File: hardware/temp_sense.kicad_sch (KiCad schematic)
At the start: 42 parts, among them U2 CD4052B, U3 MCP6004, U4 CD4052B, U5 MCP6004

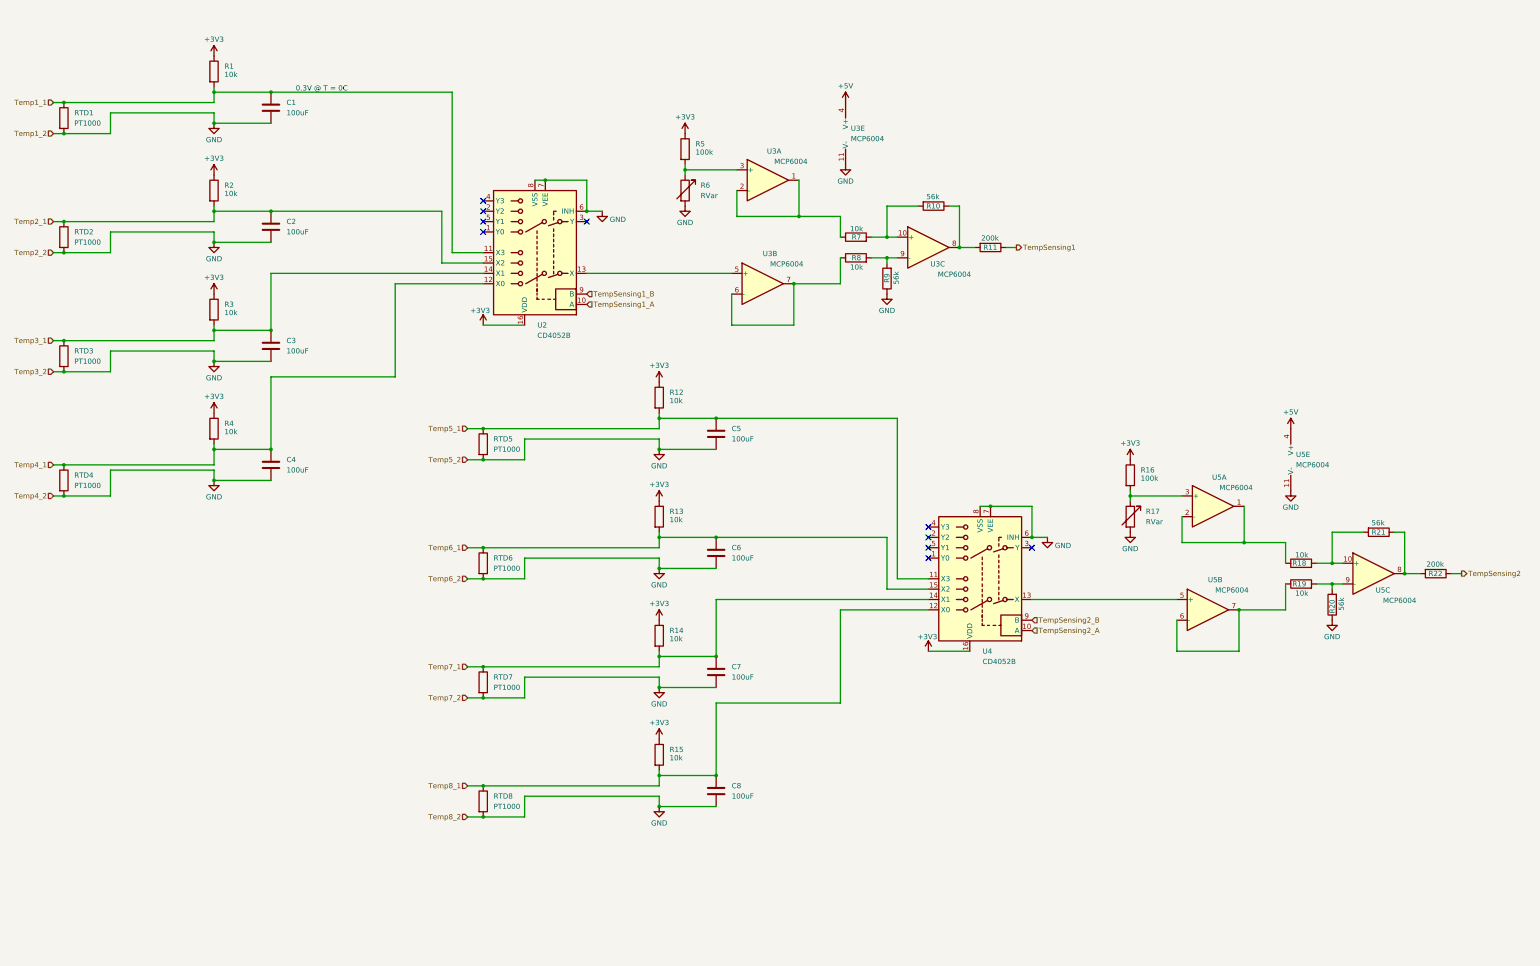
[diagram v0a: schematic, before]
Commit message: completed main board schematic
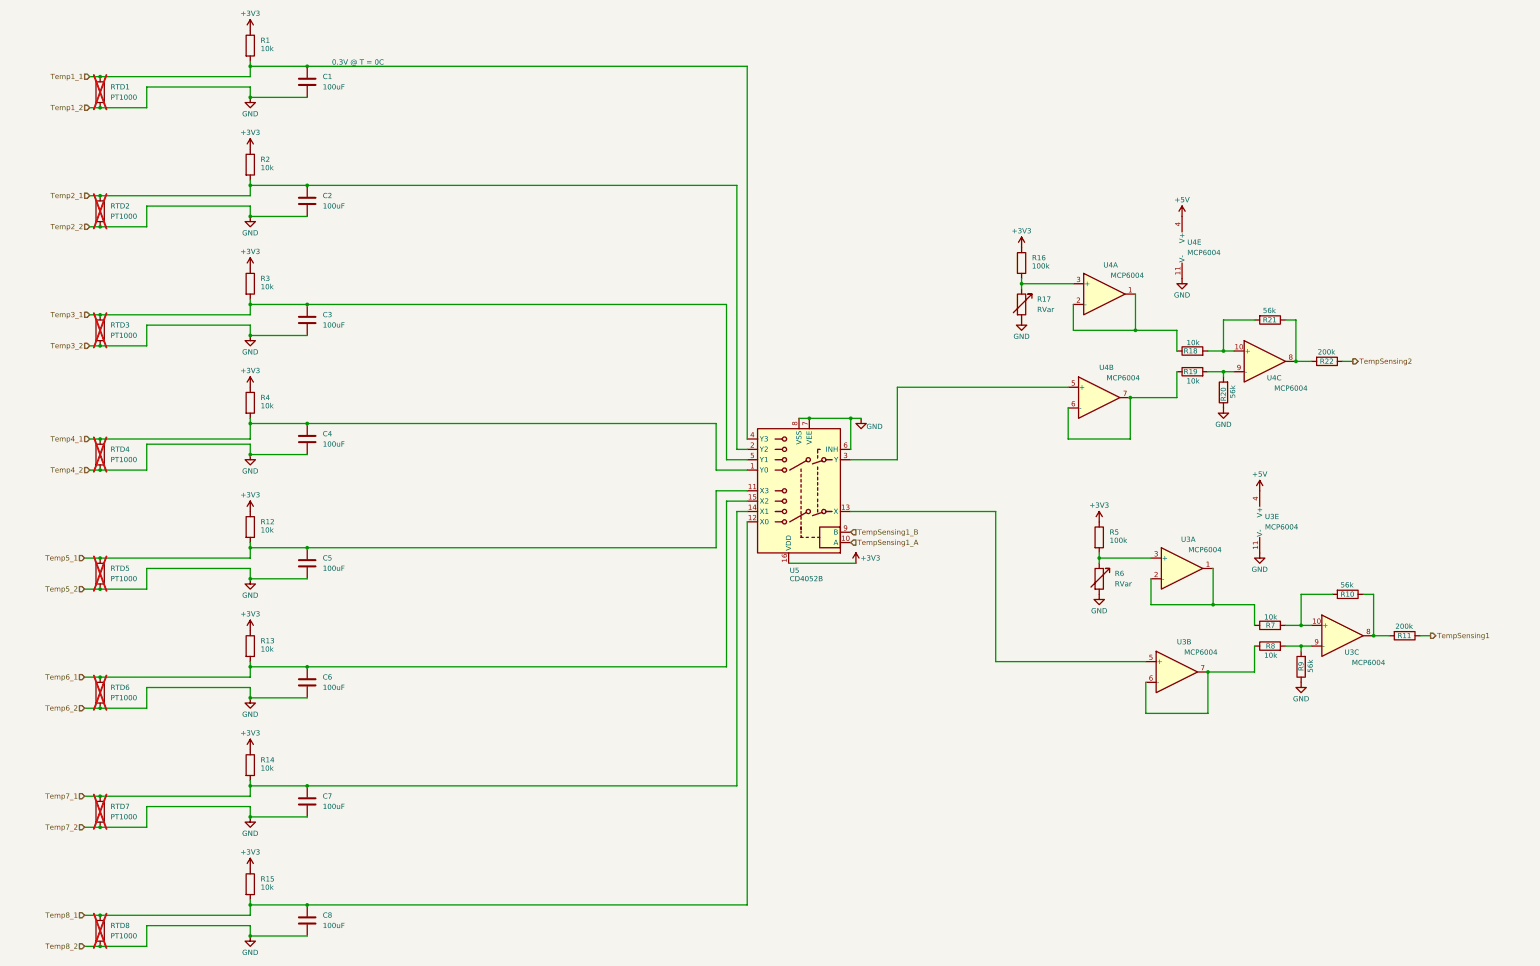
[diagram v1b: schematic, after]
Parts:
- removed U2, U4: CD4052B, symbol Analog_Switch:CD4052B
- removed U5: MCP6004, symbol Amplifier_Operational:MCP6004
- added U4: MCP6004, symbol Amplifier_Operational:MCP6004
- added U5: CD4052B, symbol Analog_Switch:CD4052B
- RTD1, RTD2, RTD3, RTD4, RTD5, RTD6, RTD7, RTD8: now not fitted
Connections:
- net +3V3: now also U5.16 (VDD)
- net +5V: now also U4.4 (V+)
- net GND: now also U4.11 (V-), U5.6 (INH), U5.7 (VEE), U5.8 (VSS)
- net Temp1_1: now also U5.4 (Y3)
- net Temp2_1: now also U5.2 (Y2)
- net Temp3_1: now also U5.5 (Y1)
- net Temp4_1: now also U5.1 (Y0)
- net Temp5_1: now also U5.11 (X3)
- net Temp6_1: now also U5.15 (X2)
- net Temp7_1: now also U5.14 (X1)
- net Temp8_1: now also U5.12 (X0)
- net TempSensing1_A: now also U5.10 (A)
- net TempSensing1_B: now also U5.9 (B)
- net at R16.2, R17.1: now also U4.3 (+)
- net at R18.1: now also U4.1, U4.2 (-)
- net at R18.2, R21.2: now also U4.10 (+)
- net at R19.1: now also U4.6 (-), U4.7
- net at R19.2, R20.2: now also U4.9 (-)
- net at U3.5 (+): now also U5.13 (X)
- net at R21.1, R22.2: now also U4.8
- new net: U4.5 (+), U5.3 (Y)
- no-connect marks 10 -> 0
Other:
- moved on the sheet: C1, C2, C3, C4, C5, C6, C7, C8, R1, R10, R11, R12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

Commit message: initial layout, power traces remain
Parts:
- C1, C2, C3, C4, C5, C6, C7, C8: footprint (none) -> Capacitor_SMD:C_0805_2012Metric_Pad1.18x1.45mm_HandSolder
- R1, R10, R11, R12, R13, R14, R15, R16, R18, R19, R2, R20, R21, R22, R3, R4, R5, R7, R8, R9: footprint (none) -> Resistor_SMD:R_0805_2012Metric_Pad1.20x1.40mm_HandSolder
- R17, R6: footprint (none) -> Potentiometer_THT:Potentiometer_Bourns_3296W_Vertical
- U3, U4: footprint (none) -> Package_SO:SOIC-14_3.9x8.7mm_P1.27mm
- U5: footprint (none) -> Package_SO:TSSOP-16_4.4x5mm_P0.65mm

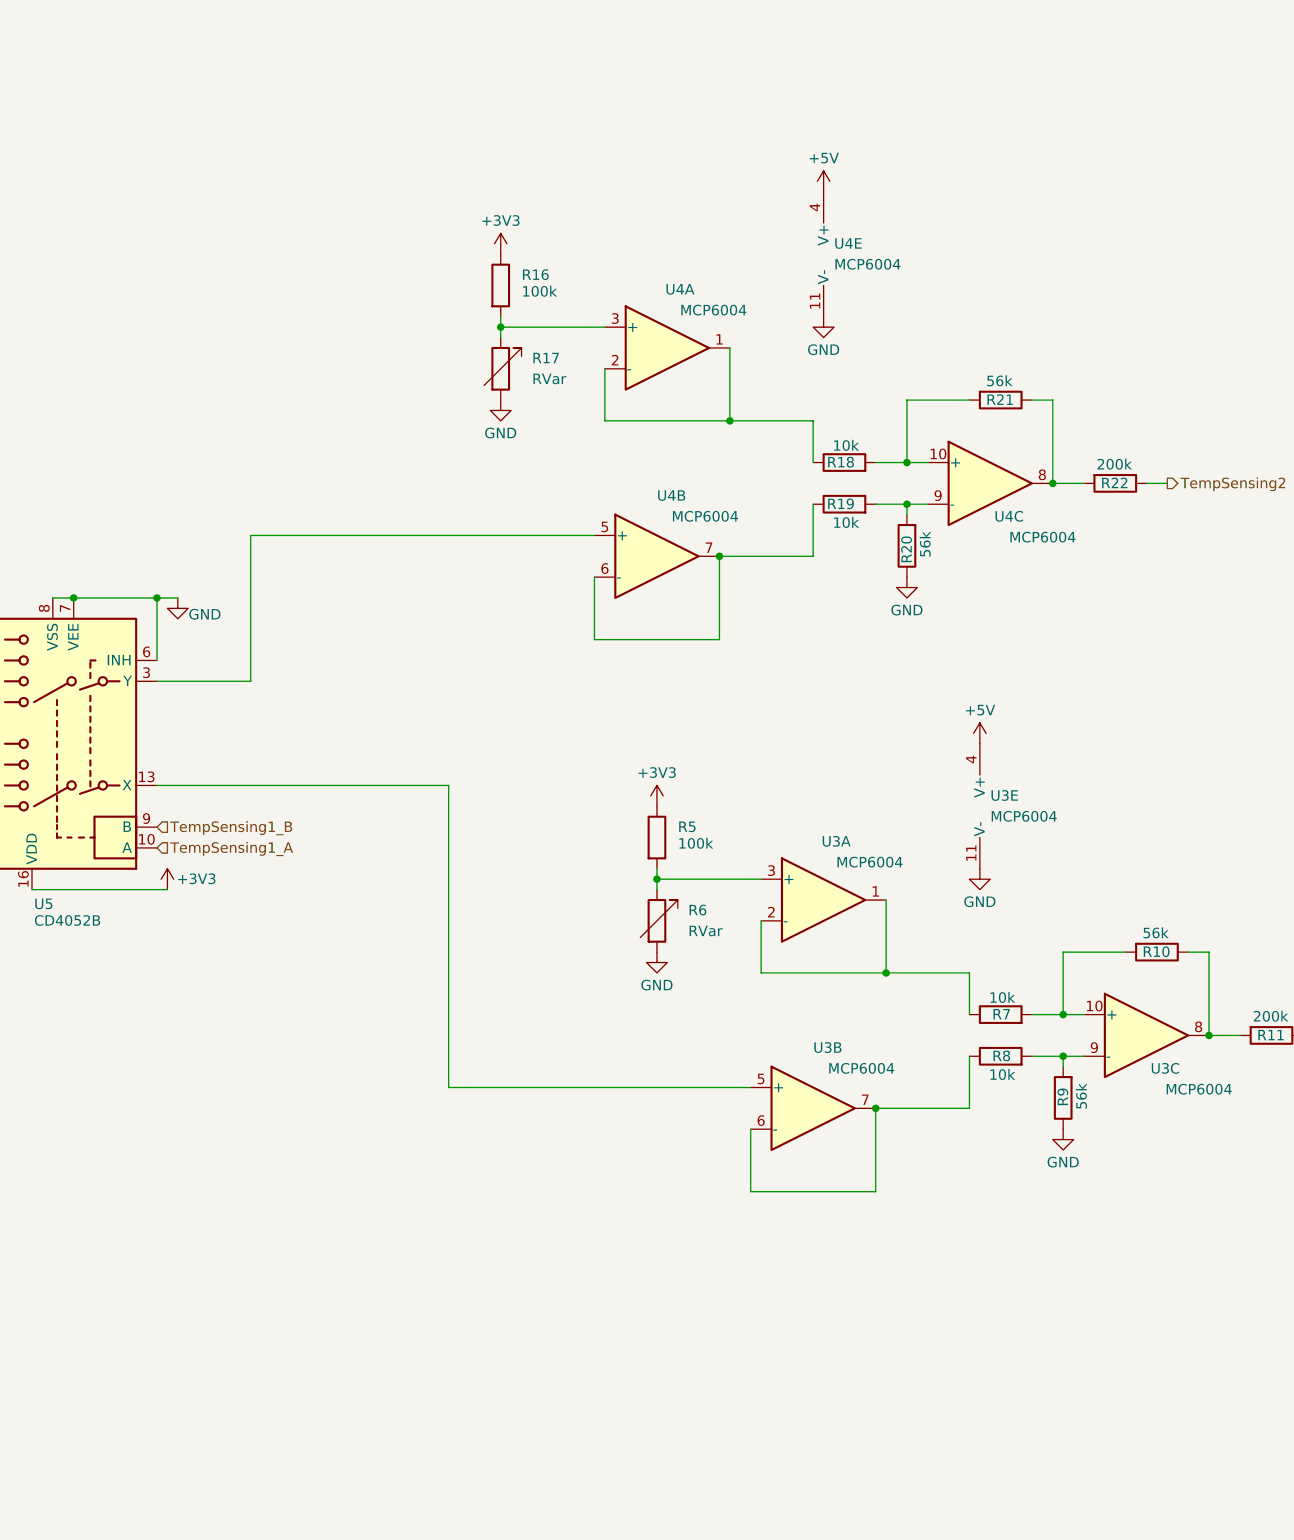
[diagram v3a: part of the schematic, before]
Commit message: Finished Layout and routing
* Flipped CAN transceiver upside down on schematic
* Moved CAN transceiver nearer to J13 and MCU CAN pins
* Moved 5V DCDC caps nearer to 5V DCDC
* Moved Silkscreen out from under U9
* Moved J2 and J1 to prevent plugging 12V into a temp sensor connector
* Change +3.3V to +3V3 to match MCU page
* Changed Current Sense circuit to use U4D, sharing with Temp Sense (for easier assembly)
* Placed Unused MCP6004s on schematic and connected them per datasheet fig 4-5
* Remove connections to HV- in Current Sensing (Replaced with GND)
* Tightened up Temp and Current Sense amplifier layouts
* Swap U15A with U15D for easier routing
* Added buffer to voltage sense circuit because filter stage could significantly load the voltage divider
* Added a smattering of decoupling caps
* Finished Layout and routing
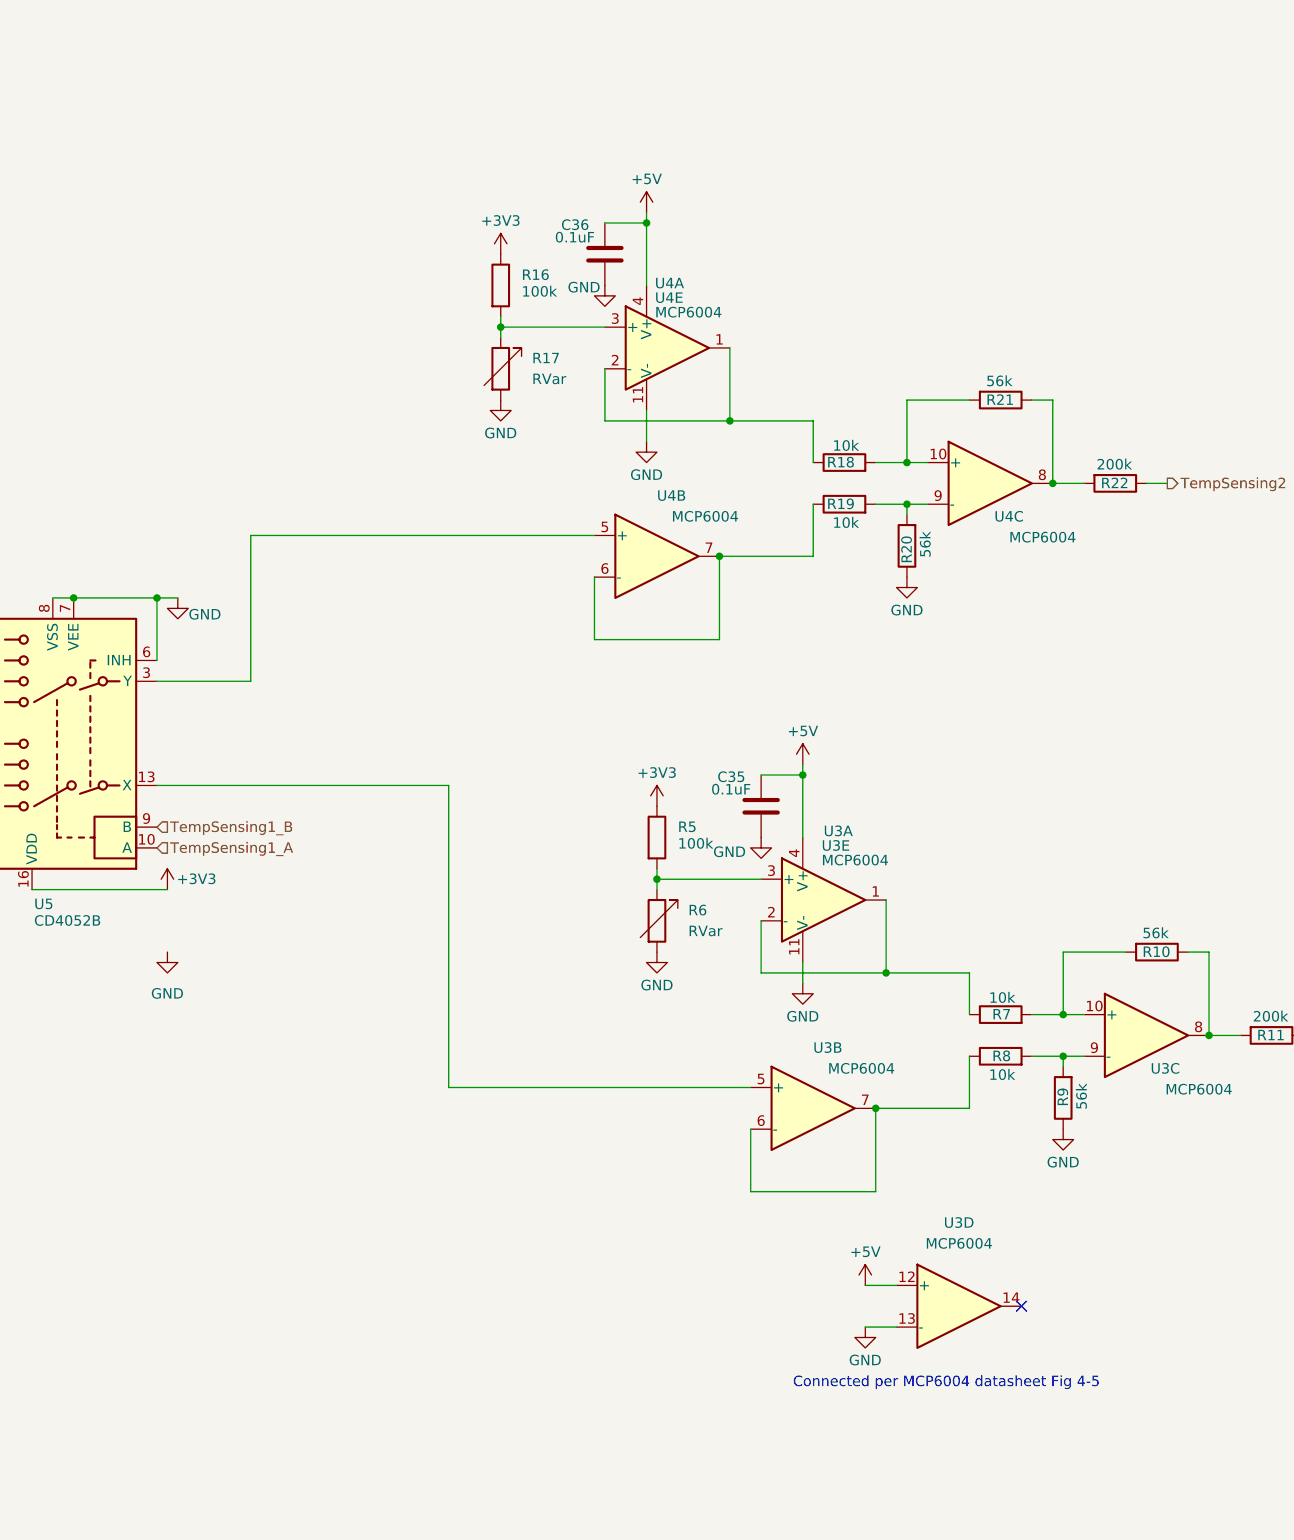
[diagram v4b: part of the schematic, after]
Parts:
- added C35, C36: 0.1uF, Capacitor_SMD:C_0805_2012Metric_Pad1.18x1.45mm_HandSolder, symbol Device:C
- C1, C2, C3, C4, C5, C6, C7, C8, R1, R10, R11, R12, R13, R14, R15, R16, R18, R19, R2, R20, R21, R22, R3, R4, R5, R7, R8, R9: KiLib_Generator (none) -> SMD_2terminal_chip_molded
- R17, R6: KiLib_Generator (none) -> potentiometer/THT
- U3, U4, U5: KiLib_Generator (none) -> package/gullwing
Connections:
- net +5V: now also U3.12 (+), C35.1, C36.1
- net GND: now also U3.13 (-), C35.2, C36.2
- no-connect marks 0 -> 1
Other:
- note added: "Connected per MCP6004 datasheet Fig 4-5"
- moved on the sheet: U3E, U4E

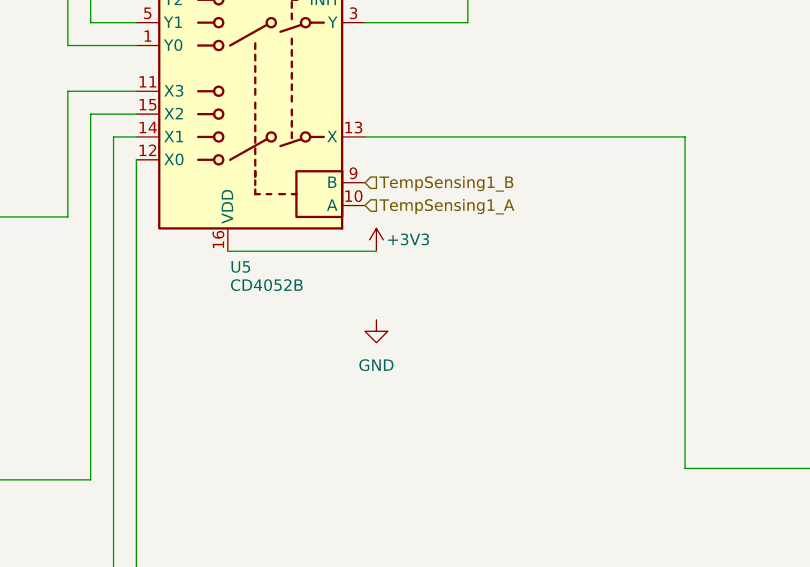
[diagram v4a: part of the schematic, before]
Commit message: Fix up silkscreen, testpoints, and one more decoupler
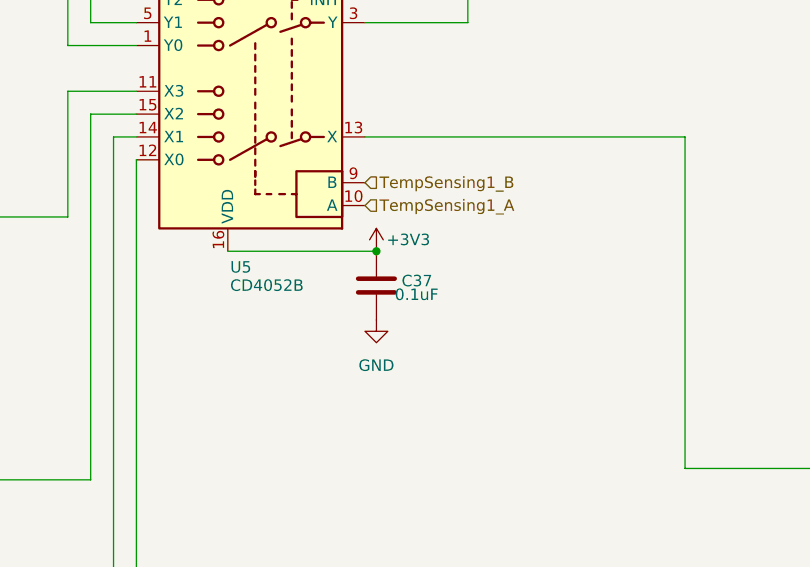
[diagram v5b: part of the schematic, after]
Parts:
- added C37: 0.1uF, Capacitor_SMD:C_0805_2012Metric_Pad1.18x1.45mm_HandSolder, symbol Device:C
- added unit 4 of U3
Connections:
- net +3V3: now also C37.1
- net +5V: now also U3.12 (+); no longer U3.12 (+)
- net GND: now also C37.2, U3.13 (-); no longer U3.13 (-)
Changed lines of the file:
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@@
 	)
 	(junction
+		(at 229.87 161.29)
+		(diameter 0)
+		(color 0 0 0 0)
+	)
+	(junction
 		(at 307.34 147.32)
 		(diameter 0)
@@
 					(unit 1)
 				)
+			)
+		)
+	)
+	(symbol
+		(lib_id "Device:C")
+		(at 229.87 165.1 0)
+		(mirror y)
+		(unit 1)
+		(body_style 1)
+		(exclude_from_sim no)
+		(in_bom yes)
+		(on_board yes)
+		(in_pos_files yes)
+		(dnp no)
+		(property "Reference" "C37"
+			(at 232.664 164.592 0)
+			(show_name no)
+			(do_not_autoplace no)
+			(effects
+				(font
+					(size 1.27 1.27)
+				)
+				(justify right)
+			)
+		)
+		(property "Value" "0.1uF"
+			(at 231.902 166.116 0)
+			(show_name no)
+			(do_not_autoplace no)
+			(effects
+				(font
+					(size 1.27 1.27)
+				)
+				(justify right)
+			)
+		)
+		(property "Footprint" "Capacitor_SMD:C_0805_2012Metric_Pad1.18x1.45mm_HandSolder"
+			(at 228.9048 168.91 0)
+			(hide yes)
+			(show_name no)
+			(do_not_autoplace no)
+			(effects
+				(font
+					(size 1.27 1.27)
+				)
+			)
+		)
+		(property "Datasheet" ""
+			(at 229.87 165.1 0)
+			(hide yes)
+			(show_name no)
+			(do_not_autoplace no)
+			(effects
+				(font
+					(size 1.27 1.27)
+				)
+			)
+		)
+		(property "Description" "Unpolarized capacitor"
+			(at 229.87 165.1 0)
+			(hide yes)
+			(show_name no)
+			(do_not_autoplace no)
+			(effects
+				(font
+					(size 1.27 1.27)
+				)
+			)
+		)
+		(property "KiLib_Generator" "SMD_2terminal_chip_molded"
+			(at 229.87 165.1 0)
+			(hide yes)
+			(show_name no)
+			(do_not_autoplace no)
+			(effects
+				(font
+					(size 1.27 1.27)
+				)
+			)
+		)
+		(pin "1"
+		)
+		(pin "2"
+		)
+		(instances
+			(project "ece129_discharger"
+				(path "/553a23ec-442a-4f98-939d-2d5634a662f5/7756f6ce-96a2-41f3-8f50-742d0a0e9d47"
+					(reference "C37")
+					(unit 1)
+				)
